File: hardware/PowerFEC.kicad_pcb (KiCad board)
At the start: 2 copper layers, 24 x 27.9 mm, 23 parts, among them J1 B2B-XH-A, P1 105444-0001, U1 PIC16F1455, U2 AP22652, U3 ZXCT1009

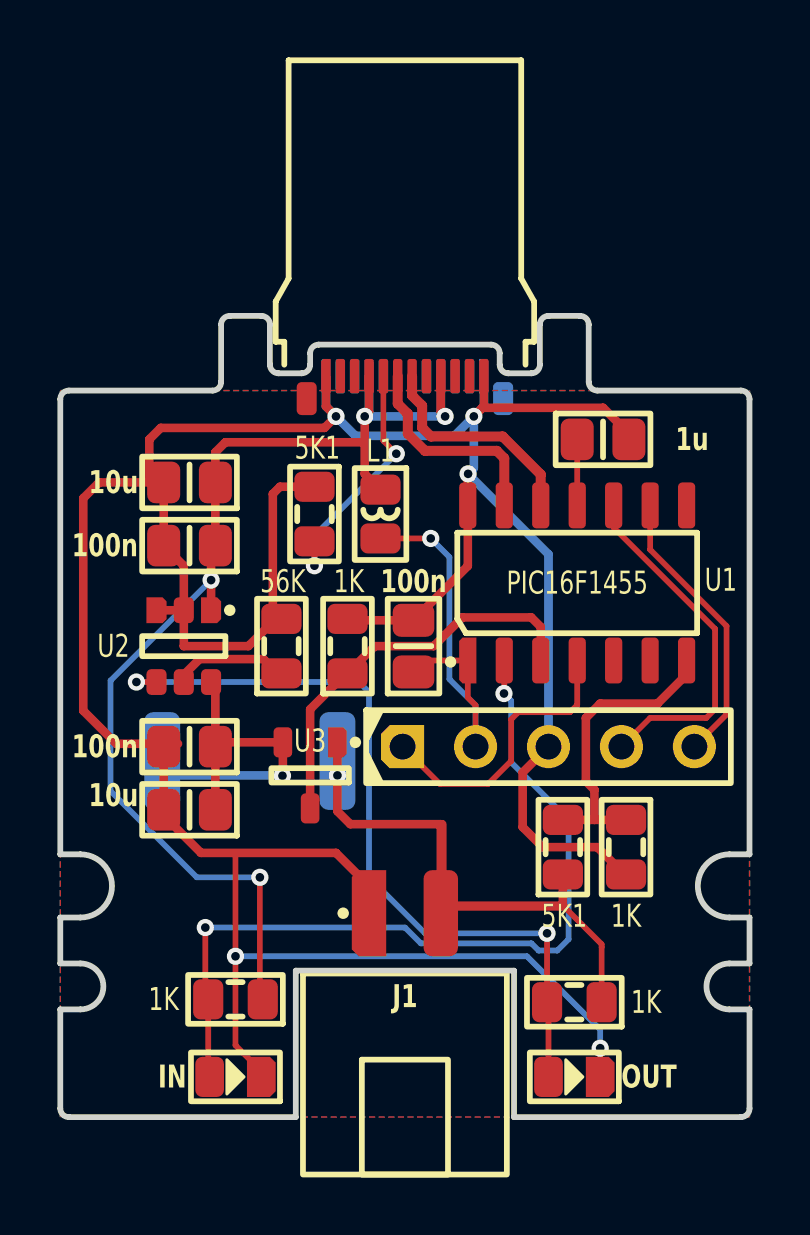
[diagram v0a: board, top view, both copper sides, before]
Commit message: Added POWER_EN line
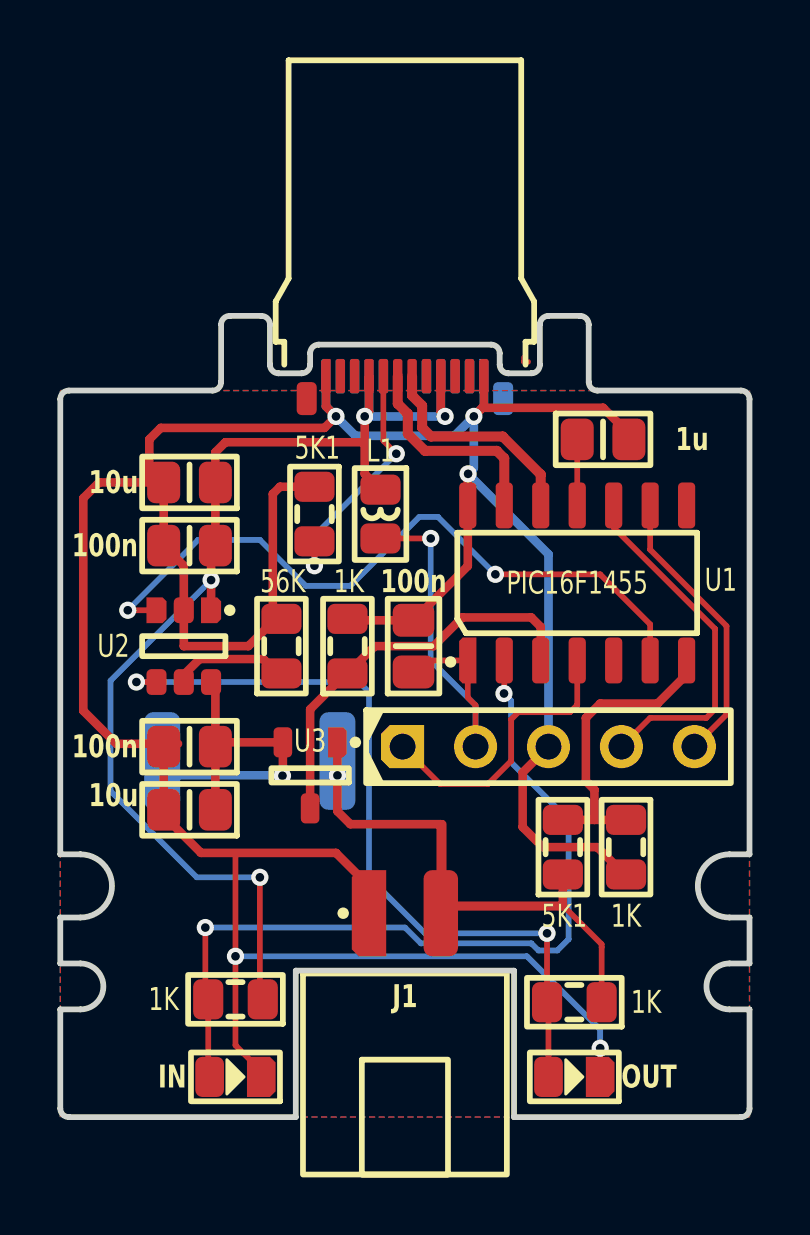
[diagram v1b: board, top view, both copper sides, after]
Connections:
- U1 pad 6: (no net) -> POWER_EN
- U2 pad 3: GND -> POWER_EN
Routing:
- net POWER_EN: track 0.00 -> 24.7 mm, vias 0 -> 2
- net GND: track 121.7 -> 120.7 mm
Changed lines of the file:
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@@
   (net 16 "LED_OUT")
   (net 17 "Vsw")
+  (net 18 "POWER_EN")
   (footprint "Medo64:R (0805)" (layer "F.Cu")
     (at 37.9 43.9 180)
@@
       (thermal_bridge_angle 45))
     (pad "6" smd roundrect (at -2.7 2.54 90) (size 1.6 0.6) (layers "F.Cu" "F.Paste" "F.Mask") (roundrect_rratio 0.25)
-      (thermal_bridge_angle 45))
+      (net 18 "POWER_EN") (thermal_bridge_angle 45))
     (pad "7" smd roundrect (at -2.7 3.81 90) (size 1.6 0.6) (layers "F.Cu" "F.Paste" "F.Mask") (roundrect_rratio 0.25)
       (net 14 "Vadc") (thermal_bridge_angle 45))
@@
     (pad "3" smd roundrect (at -1.25 0.95 270) (size 0.9 0.7) (layers "F.Cu" "F.Paste" "F.Mask") (roundrect_rratio 0.25)
       (chamfer_ratio 0.2) (chamfer top_left top_right)
-      (net 4 "GND") (thermal_bridge_angle 45))
+      (net 18 "POWER_EN") (thermal_bridge_angle 45))
     (pad "4" smd roundrect (at 1.25 0.95 270) (size 0.9 0.7) (layers "F.Cu" "F.Paste" "F.Mask") (roundrect_rratio 0.25)
       (net 16 "LED_OUT") (thermal_bridge_angle 45))
@@
     (effects (font (size 0.8 0.6) (thickness 0.15) bold) (justify mirror))
   )
+  (segment (start 36.15 21.45) (end 36.15 21.6) (width 0.2) (layer "F.Cu") (net 0))
+  (segment (start 36.15 21.6) (end 36.28761 21.6) (width 0.2) (layer "F.Cu") (net 0))
   (segment (start 28.85 28.699998) (end 28.850002 28.7) (width 0.2) (layer "F.Cu") (net 1))
   (segment (start 31.25 22.1) (end 31.25 24.35) (width 0.2) (layer "F.Cu") (net 1))
@@
   (segment (start 27 46.3) (end 26.1 45.4) (width 0.2) (layer "F.Cu") (net 4))
   (segment (start 29.6 23.5) (end 29.2 23.9) (width 0.3) (layer "F.Cu") (net 4))
-  (segment (start 24.3 30.25) (end 23.35 30.25) (width 0.3) (layer "F.Cu") (net 4))
   (segment (start 24.3 28.7) (end 23.6 28) (width 0.3) (layer "F.Cu") (net 4))
   (segment (start 27.65 25.95) (end 28.85 25.95) (width 0.3) (layer "F.Cu") (net 4))
@@
   (segment (start 31.15 27.75) (end 32.9 27.75) (width 0.2) (layer "F.Cu") (net 8))
   (via (at 32.9 27.75) (size 0.6) (drill 0.3) (layers "F.Cu" "B.Cu") (net 8))
+  (segment (start 32.9 27.75) (end 32.9 32) (width 0.2) (layer "B.Cu") (net 8))
+  (segment (start 32.9 32) (end 34.46 33.56) (width 0.2) (layer "B.Cu") (net 8))
   (segment (start 34.46 33.56) (end 34.46 35) (width 0.2) (layer "B.Cu") (net 8))
-  (segment (start 32.9 27.75) (end 33.55 28.4) (width 0.2) (layer "B.Cu") (net 8))
-  (segment (start 33.55 28.4) (end 33.55 32.65) (width 0.2) (layer "B.Cu") (net 8))
-  (segment (start 33.55 32.65) (end 34.46 33.56) (width 0.2) (layer "B.Cu") (net 8))
   (segment (start 34.9 36.3) (end 35.7 35.5) (width 0.2) (layer "F.Cu") (net 9))
   (segment (start 37.75 33.8) (end 38 33.55) (width 0.2) (layer "F.Cu") (net 9))
@@
   (segment (start 27.736091 36.013909) (end 27.722182 36) (width 0.3) (layer "B.Cu") (net 17))
   (segment (start 27.722182 36) (end 23.55 36) (width 0.3) (layer "B.Cu") (net 17))
+  (segment (start 40.54 32) (end 40.54 30.74) (width 0.2) (layer "F.Cu") (net 18))
+  (segment (start 23.35 30.25) (end 22.35 30.25) (width 0.2) (layer "F.Cu") (net 18))
+  (segment (start 40.54 30.74) (end 38.8 29) (width 0.2) (layer "F.Cu") (net 18))
+  (segment (start 38.8 29) (end 35.15 29) (width 0.2) (layer "F.Cu") (net 18))
+  (via (at 35.15 29) (size 0.6) (drill 0.3) (layers "F.Cu" "B.Cu") (net 18))
+  (via (at 22.35 30.25) (size 0.6) (drill 0.3) (layers "F.Cu" "B.Cu") (net 18))
+  (segment (start 30.1 29.4) (end 32.5 27) (width 0.2) (layer "B.Cu") (net 18))
+  (segment (start 28.55 29.4) (end 30.1 29.4) (width 0.2) (layer "B.Cu") (net 18))
+  (segment (start 33.15 27) (end 35.15 29) (width 0.2) (layer "B.Cu") (net 18))
+  (segment (start 24.8 27.8) (end 26.95 27.8) (width 0.2) (layer "B.Cu") (net 18))
+  (segment (start 22.35 30.25) (end 24.8 27.8) (width 0.2) (layer "B.Cu") (net 18))
+  (segment (start 32.5 27) (end 33.15 27) (width 0.2) (layer "B.Cu") (net 18))
+  (segment (start 26.95 27.8) (end 28.55 29.4) (width 0.2) (layer "B.Cu") (net 18))
   (zone (net 4) (net_name "GND") (layers "F&B.Cu") (hatch edge 0.5)
     (connect_pads no (clearance 0.3))

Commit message: Moved LED pin to allow for FAULT check (later)
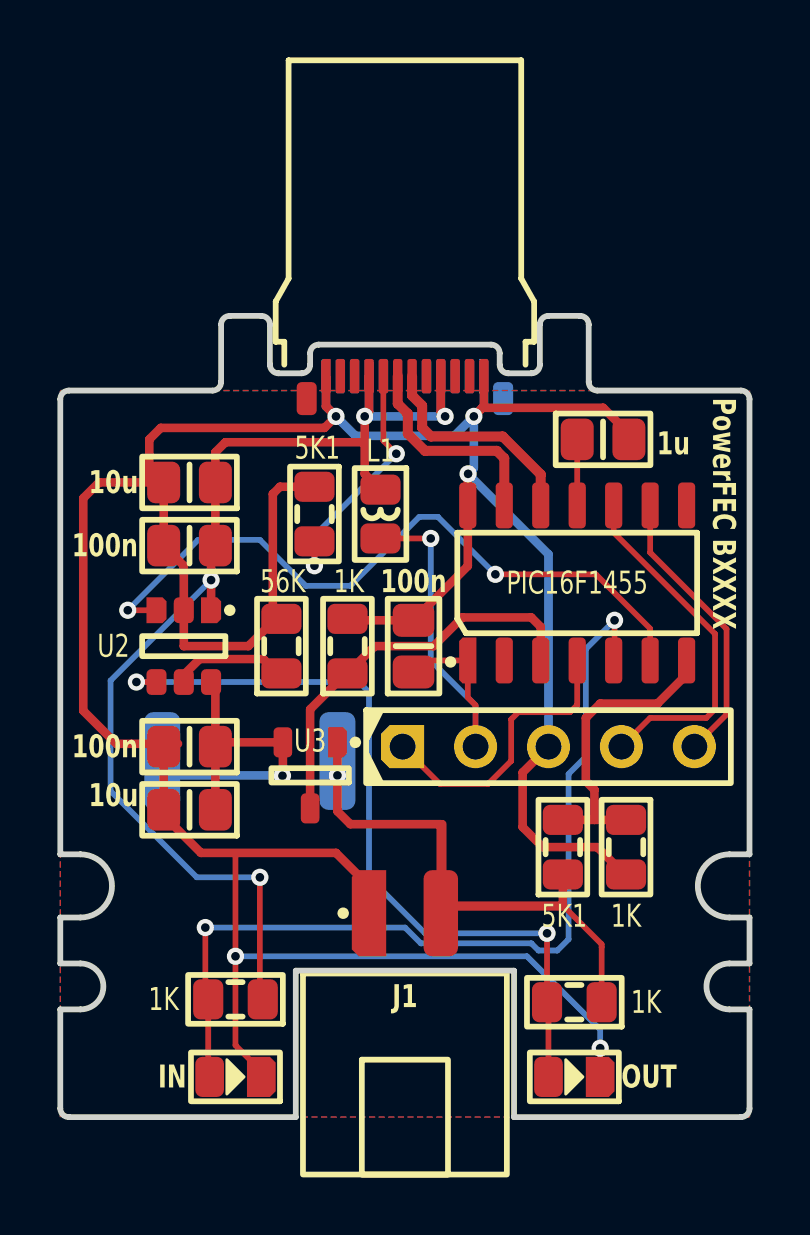
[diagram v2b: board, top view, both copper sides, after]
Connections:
- U1 pad 2: LED_IN -> (no net)
- U1 pad 5: (no net) -> LED_IN
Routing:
- net LED_IN: track 29.0 -> 31.6 mm
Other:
- board text added: "PowerFEC BXXXX"
- board text removed: "PowerFEC A"
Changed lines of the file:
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@@
     (tags "SOIC127P600X175-14AN")
     (attr smd)
-    (fp_text reference "U1" (at 0.1 5 180) (layer "F.SilkS")
+    (fp_text reference "U1" (at 0.1 5 180) (layer "F.SilkS") hide
         (effects (font (size 0.8 0.6) (thickness 0.15)))
     )
@@
       (net 8 "5V") (thermal_bridge_angle 45))
     (pad "2" smd roundrect (at -2.7 -2.54 90) (size 1.6 0.6) (layers "F.Cu" "F.Paste" "F.Mask") (roundrect_rratio 0.25)
-      (net 6 "LED_IN") (thermal_bridge_angle 45))
+      (thermal_bridge_angle 45))
     (pad "3" smd roundrect (at -2.7 -1.27 90) (size 1.6 0.6) (layers "F.Cu" "F.Paste" "F.Mask") (roundrect_rratio 0.25)
       (net 15 "Iadc") (thermal_bridge_angle 45))
@@
       (net 9 "ICSP_VPP") (thermal_bridge_angle 45))
     (pad "5" smd roundrect (at -2.7 1.27 90) (size 1.6 0.6) (layers "F.Cu" "F.Paste" "F.Mask") (roundrect_rratio 0.25)
-      (thermal_bridge_angle 45))
+      (net 6 "LED_IN") (thermal_bridge_angle 45))
     (pad "6" smd roundrect (at -2.7 2.54 90) (size 1.6 0.6) (layers "F.Cu" "F.Paste" "F.Mask") (roundrect_rratio 0.25)
       (net 18 "POWER_EN") (thermal_bridge_angle 45))
@@
         (effects (font (size 0.8 0.6) (thickness 0.15) bold))
     )
-    (fp_text value "1u" (at 3.1 0 180) (layer "F.SilkS")
+    (fp_text value "1u" (at 2.45 0.15 180) (layer "F.SilkS")
         (effects (font (size 0.8 0.6) (thickness 0.15) bold))
     )
@@
   (gr_circle locked (center 20.7 39.85) (end 23.15 39.85)
     (stroke (width 0.01) (type solid)) (fill none) (layer "Margin"))
-  (gr_text "PowerFEC A" (at 32 42) (layer "B.SilkS")
-    (effects (font (size 0.8 0.6) (thickness 0.15) bold) (justify mirror))
-  )
-  (segment (start 36.15 21.45) (end 36.15 21.6) (width 0.2) (layer "F.Cu") (net 0))
-  (segment (start 36.15 21.6) (end 36.28761 21.6) (width 0.2) (layer "F.Cu") (net 0))
+  (gr_text "PowerFEC BXXXX" (at 43.1 22.85 -90) (layer "F.SilkS")
+    (effects (font (size 0.8 0.6) (thickness 0.15) bold) (justify left))
+  )
   (segment (start 28.85 28.699998) (end 28.850002 28.7) (width 0.2) (layer "F.Cu") (net 1))
   (segment (start 31.25 22.1) (end 31.25 24.35) (width 0.2) (layer "F.Cu") (net 1))
@@
   (segment (start 29.65 37.25) (end 29.65 34.85) (width 0.3) (layer "F.Cu") (net 5))
   (via (at 29.65 36) (size 0.6) (drill 0.3) (layers "F.Cu" "B.Cu") (net 5))
-  (segment (start 35.46 33.14) (end 35.45 33.15) (width 0.2) (layer "F.Cu") (net 6))
+  (segment (start 39.3 30.6) (end 39.3 31.97) (width 0.2) (layer "F.Cu") (net 6))
   (segment (start 25.05 43.7) (end 25.05 41.3) (width 0.2) (layer "F.Cu") (net 6))
   (segment (start 25.15 43.8) (end 25.05 43.7) (width 0.2) (layer "F.Cu") (net 6))
-  (segment (start 35.46 32) (end 35.46 33.14) (width 0.2) (layer "F.Cu") (net 6))
   (segment (start 25.15 46.45) (end 25.15 43.8) (width 0.2) (layer "F.Cu") (net 6))
   (segment (start 25.2 46.5) (end 25.15 46.45) (width 0.2) (layer "F.Cu") (net 6))
-  (via (at 35.45 33.15) (size 0.6) (drill 0.3) (layers "F.Cu" "B.Cu") (net 6))
+  (segment (start 39.3 31.97) (end 39.27 32) (width 0.2) (layer "F.Cu") (net 6))
   (via (at 25.05 41.3) (size 0.6) (drill 0.3) (layers "F.Cu" "B.Cu") (net 6))
+  (via (at 39.3 30.6) (size 0.6) (drill 0.3) (layers "F.Cu" "B.Cu") (net 6))
   (segment (start 32.555026 41.85) (end 36.405025 41.85) (width 0.2) (layer "B.Cu") (net 6))
+  (segment (start 37.307107 42.1) (end 37.7 41.707107) (width 0.2) (layer "B.Cu") (net 6))
+  (segment (start 25.05 41.3) (end 32.005026 41.3) (width 0.2) (layer "B.Cu") (net 6))
+  (segment (start 37.7 41.707107) (end 37.7 35.95) (width 0.2) (layer "B.Cu") (net 6))
+  (segment (start 38.3 35.35) (end 38.3 31.6) (width 0.2) (layer "B.Cu") (net 6))
+  (segment (start 32.005026 41.3) (end 32.555026 41.85) (width 0.2) (layer "B.Cu") (net 6))
+  (segment (start 36.655025 42.1) (end 37.307107 42.1) (width 0.2) (layer "B.Cu") (net 6))
+  (segment (start 38.3 31.6) (end 39.3 30.6) (width 0.2) (layer "B.Cu") (net 6))
+  (segment (start 37.7 35.95) (end 38.3 35.35) (width 0.2) (layer "B.Cu") (net 6))
   (segment (start 36.405025 41.85) (end 36.655025 42.1) (width 0.2) (layer "B.Cu") (net 6))
-  (segment (start 35.7 33.4) (end 35.45 33.15) (width 0.2) (layer "B.Cu") (net 6))
-  (segment (start 37.307107 42.1) (end 37.7 41.707107) (width 0.2) (layer "B.Cu") (net 6))
-  (segment (start 37.7 37.55) (end 35.7 35.55) (width 0.2) (layer "B.Cu") (net 6))
-  (segment (start 32.005026 41.3) (end 32.555026 41.85) (width 0.2) (layer "B.Cu") (net 6))
-  (segment (start 35.7 35.55) (end 35.7 33.4) (width 0.2) (layer "B.Cu") (net 6))
-  (segment (start 37.7 41.707107) (end 37.7 37.55) (width 0.2) (layer "B.Cu") (net 6))
-  (segment (start 36.655025 42.1) (end 37.307107 42.1) (width 0.2) (layer "B.Cu") (net 6))
-  (segment (start 25.05 41.3) (end 32.005026 41.3) (width 0.2) (layer "B.Cu") (net 6))
   (segment (start 24.85 31.95) (end 27.075 31.95) (width 0.3) (layer "F.Cu") (net 7))
   (segment (start 27.075 31.95) (end 27.575 32.45) (width 0.3) (layer "F.Cu") (net 7))
@@
   (segment (start 35.7 35.5) (end 35.7 34.05) (width 0.2) (layer "F.Cu") (net 9))
   (segment (start 35.95 33.8) (end 37.75 33.8) (width 0.2) (layer "F.Cu") (net 9))
+  (segment (start 43.2 33.88) (end 43.2 30.9) (width 0.2) (layer "F.Cu") (net 10))
   (segment (start 42.08 35) (end 43.2 33.88) (width 0.2) (layer "F.Cu") (net 10))
-  (segment (start 40.54 28.14) (end 40.54 26.6) (width 0.2) (layer "F.Cu") (net 10))
-  (segment (start 43.2 30.8) (end 40.54 28.14) (width 0.2) (layer "F.Cu") (net 10))
-  (segment (start 43.2 33.88) (end 43.2 30.8) (width 0.2) (layer "F.Cu") (net 10))
-  (segment (start 39.27 27.37) (end 39.27 26.6) (width 0.2) (layer "F.Cu") (net 11))
-  (segment (start 42.8 30.9) (end 39.27 27.37) (width 0.2) (layer "F.Cu") (net 11))
-  (segment (start 42.8 33.694214) (end 42.8 30.9) (width 0.2) (layer "F.Cu") (net 11))
+  (segment (start 40.54 28.24) (end 40.54 26.6) (width 0.2) (layer "F.Cu") (net 10))
+  (segment (start 43.2 30.9) (end 40.54 28.24) (width 0.2) (layer "F.Cu") (net 10))
+  (segment (start 40.54 34) (end 42.494214 34) (width 0.2) (layer "F.Cu") (net 11))
   (segment (start 42.494214 34) (end 42.8 33.694214) (width 0.2) (layer "F.Cu") (net 11))
+  (segment (start 42.8 31.075) (end 39.27 27.545) (width 0.2) (layer "F.Cu") (net 11))
+  (segment (start 39.27 27.545) (end 39.27 26.6) (width 0.2) (layer "F.Cu") (net 11))
   (segment (start 39.54 35) (end 40.54 34) (width 0.2) (layer "F.Cu") (net 11))
-  (segment (start 40.54 34) (end 42.494214 34) (width 0.2) (layer "F.Cu") (net 11))
+  (segment (start 42.8 33.694214) (end 42.8 31.075) (width 0.2) (layer "F.Cu") (net 11))
   (segment (start 38 26.6) (end 38 24.3) (width 0.2) (layer "F.Cu") (net 12))
   (segment (start 33.25 22.1) (end 33.25 23.35) (width 0.3) (layer "F.Cu") (net 13))
@@
   (segment (start 27.736091 36.013909) (end 27.722182 36) (width 0.3) (layer "B.Cu") (net 17))
   (segment (start 27.722182 36) (end 23.55 36) (width 0.3) (layer "B.Cu") (net 17))
-  (segment (start 40.54 32) (end 40.54 30.74) (width 0.2) (layer "F.Cu") (net 18))
+  (segment (start 40.54 32) (end 40.54 30.89) (width 0.2) (layer "F.Cu") (net 18))
   (segment (start 23.35 30.25) (end 22.35 30.25) (width 0.2) (layer "F.Cu") (net 18))
-  (segment (start 40.54 30.74) (end 38.8 29) (width 0.2) (layer "F.Cu") (net 18))
-  (segment (start 38.8 29) (end 35.15 29) (width 0.2) (layer "F.Cu") (net 18))
+  (segment (start 38.65 29) (end 35.15 29) (width 0.2) (layer "F.Cu") (net 18))
+  (segment (start 40.54 30.89) (end 38.65 29) (width 0.2) (layer "F.Cu") (net 18))
   (via (at 35.15 29) (size 0.6) (drill 0.3) (layers "F.Cu" "B.Cu") (net 18))
   (via (at 22.35 30.25) (size 0.6) (drill 0.3) (layers "F.Cu" "B.Cu") (net 18))

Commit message: Added fault check pin
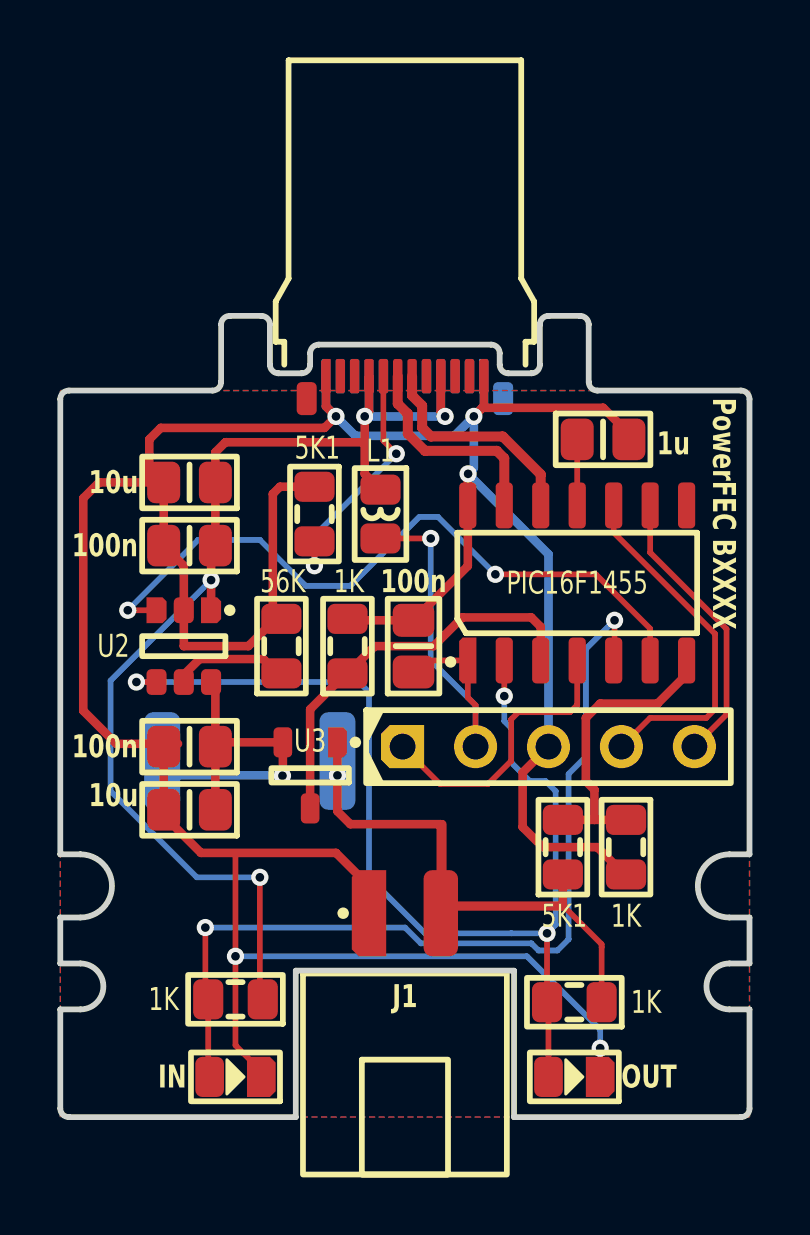
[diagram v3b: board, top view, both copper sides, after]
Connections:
- DS2 pad 2: LED_OUT -> POWER_FAULT
- R4 pad 2: LED_OUT -> POWER_FAULT
- U1 pad 2: (no net) -> POWER_FAULT
- U2 pad 4: LED_OUT -> POWER_FAULT
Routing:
- net POWER_FAULT: track 0.00 -> 38.2 mm, vias 0 -> 3
- net LED_OUT: track 27.5 -> 0.00 mm, vias 2 -> 0
